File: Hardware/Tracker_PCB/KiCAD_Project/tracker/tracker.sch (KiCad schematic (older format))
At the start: 58 parts, among them J1 RockBlock9603, J2 Switch, J3 Battery, J4 ICSP, Q1 BSS138, Q2 BSS138, SW1 SW_SPST, U1 XBee, U2 ATmega328P-AU, U3 TSR2, U4 RockBlockMechanical, U5 ublox_SAM-M8Q, U6 MIC5219-3.3YM5, Y1 16MHz

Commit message: Footprints and BOM complete.
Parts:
- removed C12, C13, C4: 10u, symbol Device:C
- added C12, C13, C4: 1-0000075, capacitors_0805:1-0000075, symbol capacitors_0805:1-0000075
- added PCB1: barepcb, lib_fp:BarePCB, symbol lib_sch:barepcb
- BT1: footprint (none) -> lib_fp:S8411-45R
- C1, C10, C11, C14, C2, C3, C5, C6, C7, C9: Populated (none) -> 1; Population 1 -> (none)
- C8: Populated (none) -> 0; Population 0 -> (none)
- D1, D2, D3, D4: footprint (none) -> LED_SMD:LED_0805_2012Metric
- F1: footprint (none) -> Fuse:Fuse_1812_4532Metric; Populated (none) -> 1
- FID1, FID2: footprint (none) -> Fiducial:Fiducial_1mm_Mask2mm; Internal Part Number (none) -> 0-0000000; Populated (none) -> 0
- H1, H2, H3, H4: footprint (none) -> MountingHole:MountingHole_3.2mm_M3_DIN965; Internal Part Number (none) -> 0-0000000; Populated (none) -> 0
- J1: footprint (none) -> lib_fp:picoblade; Internal Part Number (none) -> 1-0000790; Populated (none) -> 1
- J2: renamed from J4; footprint (none) -> Connector_PinHeader_2.54mm:PinHeader_2x03_P2.54mm_Vertical; Internal Part Number (none) -> 0-0000000; Populated (none) -> 0
- J3: renamed from J2; footprint (none) -> Connector_PinHeader_2.54mm:PinHeader_1x02_P2.54mm_Vertical; Internal Part Number (none) -> 0-0000000; Populated (none) -> 0
- J4: renamed from J3; footprint (none) -> Connector_PinHeader_2.54mm:PinHeader_1x02_P2.54mm_Vertical; Internal Part Number (none) -> 0-0000000; Populated (none) -> 0
- Q1, Q2: Internal Part Number (none) -> 1-0000340; Populated (none) -> 1
- SW1: footprint (none) -> lib_fp:SW_GF-123-0054; Internal Part Number (none) -> 1-0000786; Populated (none) -> 1
- U1: footprint (none) -> lib_fp:XBee; Internal Part Number (none) -> 1-0000785; Populated (none) -> 1
- U3: footprint (none) -> lib_fp:TSR 2-2450; Internal Part Number (none) -> 1-0000748; Populated (none) -> 1
- U4: footprint (none) -> lib_fp:RockBlock_Mechanical; Internal Part Number (none) -> 1-0000789
- Y1: footprint (none) -> lib_fp:Resonator

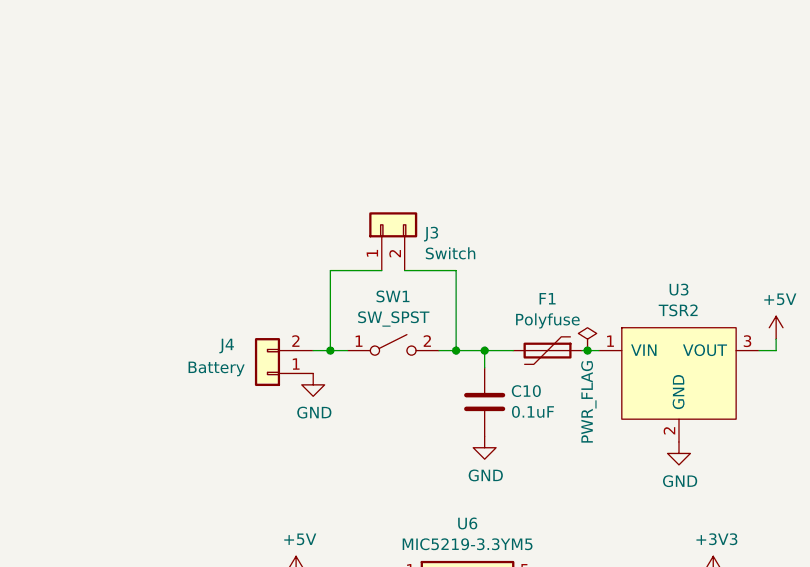
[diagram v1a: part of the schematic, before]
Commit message: Physically layout components on PCB
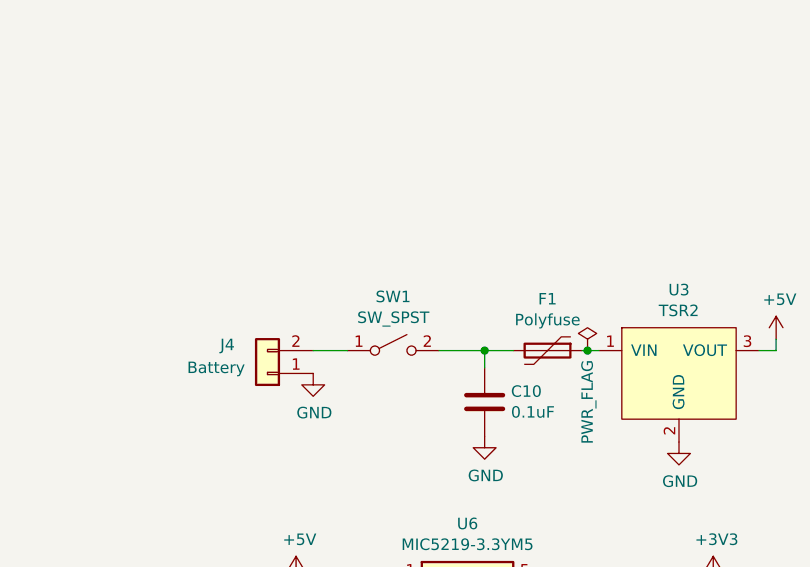
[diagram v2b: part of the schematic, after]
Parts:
- removed J3: Switch, Connector_PinHeader_2.54mm:PinHeader_1x02_P2.54mm_Vertical, symbol Connector_Generic:Conn_01x02
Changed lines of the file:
@@
 $EndComp
 $Comp
-L Connector_Generic:Conn_01x02 J3
-U 1 1 5FFB5D23
-P 1425 5500
-F 0 "J3" V 1389 5312 50  0000 R CNN
-F 1 "Switch" V 1298 5312 50  0000 R CNN
-F 2 "Connector_PinHeader_2.54mm:PinHeader_1x02_P2.54mm_Vertical" H 1425 5500 50  0001 C CNN
-F 3 "~" H 1425 5500 50  0001 C CNN
-F 4 "0-0000000" H 1425 5500 50  0001 C CNN "Internal Part Number"
-F 5 "0" H 1425 5500 50  0001 C CNN "Populated"
-	1    1425 5500
-	0    -1   -1   0
-$EndComp
-Wire Wire Line
-	1125 6050 1200 6050
-Wire Wire Line
-	1425 5700 1200 5700
-Wire Wire Line
-	1200 5700 1200 6050
-Wire Wire Line
-	1200 6050 1275 6050
-Wire Wire Line
-	1525 5700 1750 5700
-Wire Wire Line
-	1750 5700 1750 6050
-Wire Wire Line
-	1750 6050 1675 6050
-$Comp
 L power:GND #PWR031
 U 1 1 5FFB8FA4
@@
 	0    1    1    0
 $EndComp
-Connection ~ 1200 6050
 $Comp
 L capacitors_0603:1-0000007 C10
@@
 	1875 6125 1875 6050
 Wire Wire Line
-	1875 6050 1750 6050
-Connection ~ 1750 6050
-Wire Wire Line
 	1875 6050 2000 6050
 Connection ~ 1875 6050
@@
 	1    0    0    -1
 $EndComp
+Wire Wire Line
+	1125 6050 1275 6050
+Wire Wire Line
+	1675 6050 1875 6050
 $EndSCHEMATC

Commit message: Tracker hardware updates
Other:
- note added: "Cable 1-0000791\nNOTE: MUST be repinned"
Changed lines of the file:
@@
 Wire Wire Line
 	1675 6050 1875 6050
+Text Notes 8750 1225 0    50   ~ 0
+Cable 1-0000791\nNOTE: MUST be repinned
 $EndSCHEMATC

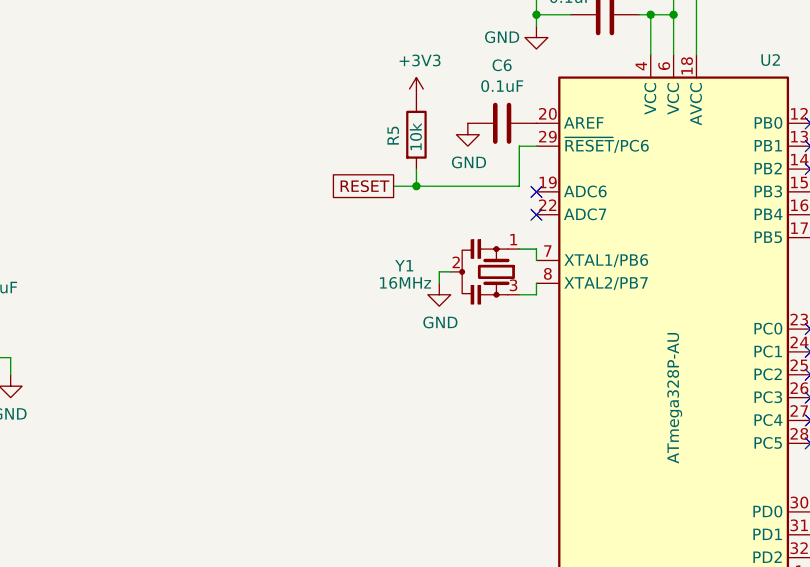
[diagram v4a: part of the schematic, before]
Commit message: Change to 8MHz Xtal
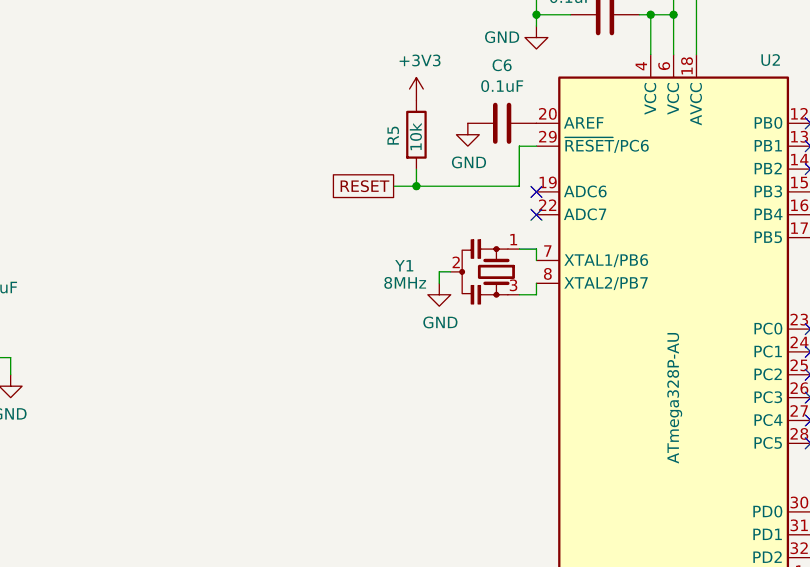
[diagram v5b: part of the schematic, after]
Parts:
- Y1: value 16MHz -> 8MHz; Internal Part Number 1-0000569 -> 1-0000721
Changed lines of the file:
@@
 P 6125 3325
 F 0 "Y1" V 6100 2925 50  0000 C CNN
-F 1 "16MHz" V 6175 2925 50  0000 C CNN
+F 1 "8MHz" V 6175 2925 50  0000 C CNN
 F 2 "lib_fp:Resonator" H 6100 3325 50  0001 C CNN
 F 3 "~" H 6100 3325 50  0001 C CNN
-F 4 "1-0000569" H 6125 3325 50  0001 C CNN "Internal Part Number"
+F 4 "1-0000721" H 6125 3325 50  0001 C CNN "Internal Part Number"
 F 5 "1" H 6125 3325 50  0001 C CNN "Populated"
 	1    6125 3325
